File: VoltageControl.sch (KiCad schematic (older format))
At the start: 7 parts

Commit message: Initial Annotation
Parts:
- gave numbers to parts that had none: 7
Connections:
- net at R201.1, RV201.3: now also U201.3 (+); no longer U201.5 (+)
- net at R202.2, R203.1: now also U201.2 (-); no longer U201.6 (-)
- net at D201.2 (K): now also U201.1; no longer U201.7
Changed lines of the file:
@@
 $EndDescr
 $Comp
-L LMV358 U?
-U 2 1 54DB1D03
+L LMV358 U201
+U 1 1 54DB1D03
 P 5850 3050
-F 0 "U?" H 5800 3250 60  0000 L CNN
+F 0 "U201" H 5800 3250 60  0000 L CNN
 F 1 "LMV358" H 5800 2800 60  0000 L CNN
 F 2 "" H 5850 3050 60  0000 C CNN
 F 3 "" H 5850 3050 60  0000 C CNN
-	2    5850 3050
+	1    5850 3050
 	1    0    0    -1
 $EndComp
 $Comp
-L R R?
+L R R201
 U 1 1 54DB1D0A
 P 3950 4250
-F 0 "R?" V 4030 4250 50  0000 C CNN
+F 0 "R201" V 4030 4250 50  0000 C CNN
 F 1 "R" V 3957 4251 50  0000 C CNN
 F 2 "" V 3880 4250 30  0000 C CNN
@@
 $EndComp
 $Comp
-L GND #PWR?
+L GND #PWR202
 U 1 1 54DB1D11
 P 5750 3600
-F 0 "#PWR?" H 5750 3350 60  0001 C CNN
+F 0 "#PWR202" H 5750 3350 60  0001 C CNN
 F 1 "GND" H 5750 3450 60  0000 C CNN
 F 2 "" H 5750 3600 60  0000 C CNN
@@
 	3950 5550 9850 5550
 $Comp
-L POT RV?
+L POT RV201
 U 1 1 54DB1D22
 P 3950 3550
-F 0 "RV?" H 3950 3450 50  0000 C CNN
+F 0 "RV201" H 3950 3450 50  0000 C CNN
 F 1 "POT" H 3950 3550 50  0000 C CNN
 F 2 "" H 3950 3550 60  0000 C CNN
@@
 Connection ~ 4100 1950
 $Comp
-L GND #PWR?
+L GND #PWR201
 U 1 1 54DB1D2C
 P 5150 2650
-F 0 "#PWR?" H 5150 2400 60  0001 C CNN
+F 0 "#PWR201" H 5150 2400 60  0001 C CNN
 F 1 "GND" H 5150 2500 60  0000 C CNN
 F 2 "" H 5150 2650 60  0000 C CNN
@@
 $EndComp
 $Comp
-L C C?
+L C C201
 U 1 1 54DB1D32
 P 5150 2400
-F 0 "C?" H 5200 2500 50  0000 L CNN
+F 0 "C201" H 5200 2500 50  0000 L CNN
 F 1 "C" H 5200 2300 50  0000 L CNN
 F 2 "" H 5188 2250 30  0000 C CNN
@@
 	6350 3050 6550 3050
 $Comp
-L DIODE D?
+L DIODE D201
 U 1 1 54DB1E38
 P 6750 3050
-F 0 "D?" H 6750 3150 40  0000 C CNN
+F 0 "D201" H 6750 3150 40  0000 C CNN
 F 1 "DIODE" H 6750 2950 40  0000 C CNN
 F 2 "" H 6750 3050 60  0000 C CNN
@@
 $EndComp
 $Comp
-L R R?
+L R R202
 U 1 1 54DB1EC2
 P 8700 3450
-F 0 "R?" V 8780 3450 50  0000 C CNN
+F 0 "R202" V 8780 3450 50  0000 C CNN
 F 1 "9K" V 8707 3451 50  0000 C CNN
 F 2 "" V 8630 3450 30  0000 C CNN
@@
 $EndComp
 $Comp
-L R R?
+L R R203
 U 1 1 54DB1F3A
 P 8700 4300
-F 0 "R?" V 8780 4300 50  0000 C CNN
+F 0 "R203" V 8780 4300 50  0000 C CNN
 F 1 "1K" V 8707 4301 50  0000 C CNN
 F 2 "" V 8630 4300 30  0000 C CNN

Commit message: Preliminary association of components and placement into layout.
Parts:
- C201, R201, R202, R203: footprint (none) -> SMD_Packages:SMD-0805
- D201: footprint (none) -> SMD_Packages:SOD-523; MPN (none) -> 1N4148WT-7
- RV201: footprint (none) -> Potentiometers:Potentiometer_WirePads_largePads
- U201: footprint (none) -> SMD_Packages:SOIC-8-N; MPN (none) -> Value
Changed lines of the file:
@@
 F 0 "U201" H 5800 3250 60  0000 L CNN
 F 1 "LMV358" H 5800 2800 60  0000 L CNN
-F 2 "" H 5850 3050 60  0000 C CNN
-F 3 "" H 5850 3050 60  0000 C CNN
+F 2 "SMD_Packages:SOIC-8-N" H 5850 3050 60  0001 C CNN
+F 3 "" H 5850 3050 60  0001 C CNN
+F 4 "Value" H 5850 3050 60  0001 C CNN "MPN"
 	1    5850 3050
 	1    0    0    -1
@@
 F 0 "R201" V 4030 4250 50  0000 C CNN
 F 1 "R" V 3957 4251 50  0000 C CNN
-F 2 "" V 3880 4250 30  0000 C CNN
+F 2 "SMD_Packages:SMD-0805" V 3880 4250 30  0001 C CNN
 F 3 "" H 3950 4250 30  0000 C CNN
 	1    3950 4250
@@
 $EndComp
 $Comp
-L GND #PWR202
+L GND #PWR03
 U 1 1 54DB1D11
 P 5750 3600
-F 0 "#PWR202" H 5750 3350 60  0001 C CNN
+F 0 "#PWR03" H 5750 3350 60  0001 C CNN
 F 1 "GND" H 5750 3450 60  0000 C CNN
 F 2 "" H 5750 3600 60  0000 C CNN
@@
 F 0 "RV201" H 3950 3450 50  0000 C CNN
 F 1 "POT" H 3950 3550 50  0000 C CNN
-F 2 "" H 3950 3550 60  0000 C CNN
+F 2 "Potentiometers:Potentiometer_WirePads_largePads" H 3950 3550 60  0001 C CNN
 F 3 "" H 3950 3550 60  0000 C CNN
 	1    3950 3550
@@
 Connection ~ 4100 1950
 $Comp
-L GND #PWR201
+L GND #PWR04
 U 1 1 54DB1D2C
 P 5150 2650
-F 0 "#PWR201" H 5150 2400 60  0001 C CNN
+F 0 "#PWR04" H 5150 2400 60  0001 C CNN
 F 1 "GND" H 5150 2500 60  0000 C CNN
 F 2 "" H 5150 2650 60  0000 C CNN
@@
 F 0 "C201" H 5200 2500 50  0000 L CNN
 F 1 "C" H 5200 2300 50  0000 L CNN
-F 2 "" H 5188 2250 30  0000 C CNN
+F 2 "SMD_Packages:SMD-0805" H 5188 2250 30  0001 C CNN
 F 3 "" H 5150 2400 60  0000 C CNN
 	1    5150 2400
@@
 F 0 "D201" H 6750 3150 40  0000 C CNN
 F 1 "DIODE" H 6750 2950 40  0000 C CNN
-F 2 "" H 6750 3050 60  0000 C CNN
-F 3 "" H 6750 3050 60  0000 C CNN
+F 2 "SMD_Packages:SOD-523" H 6750 3050 60  0001 C CNN
+F 3 "http://www.diodes.com/datasheets/ds30396.pdf" H 6750 3050 60  0001 C CNN
+F 4 "1N4148WT-7" H 6750 3050 60  0001 C CNN "MPN"
 	1    6750 3050
 	-1   0    0    1
@@
 F 0 "R202" V 8780 3450 50  0000 C CNN
 F 1 "9K" V 8707 3451 50  0000 C CNN
-F 2 "" V 8630 3450 30  0000 C CNN
+F 2 "SMD_Packages:SMD-0805" V 8630 3450 30  0001 C CNN
 F 3 "" H 8700 3450 30  0000 C CNN
 	1    8700 3450
@@
 F 0 "R203" V 8780 4300 50  0000 C CNN
 F 1 "1K" V 8707 4301 50  0000 C CNN
-F 2 "" V 8630 4300 30  0000 C CNN
+F 2 "SMD_Packages:SMD-0805" V 8630 4300 30  0001 C CNN
 F 3 "" H 8700 4300 30  0000 C CNN
 	1    8700 4300

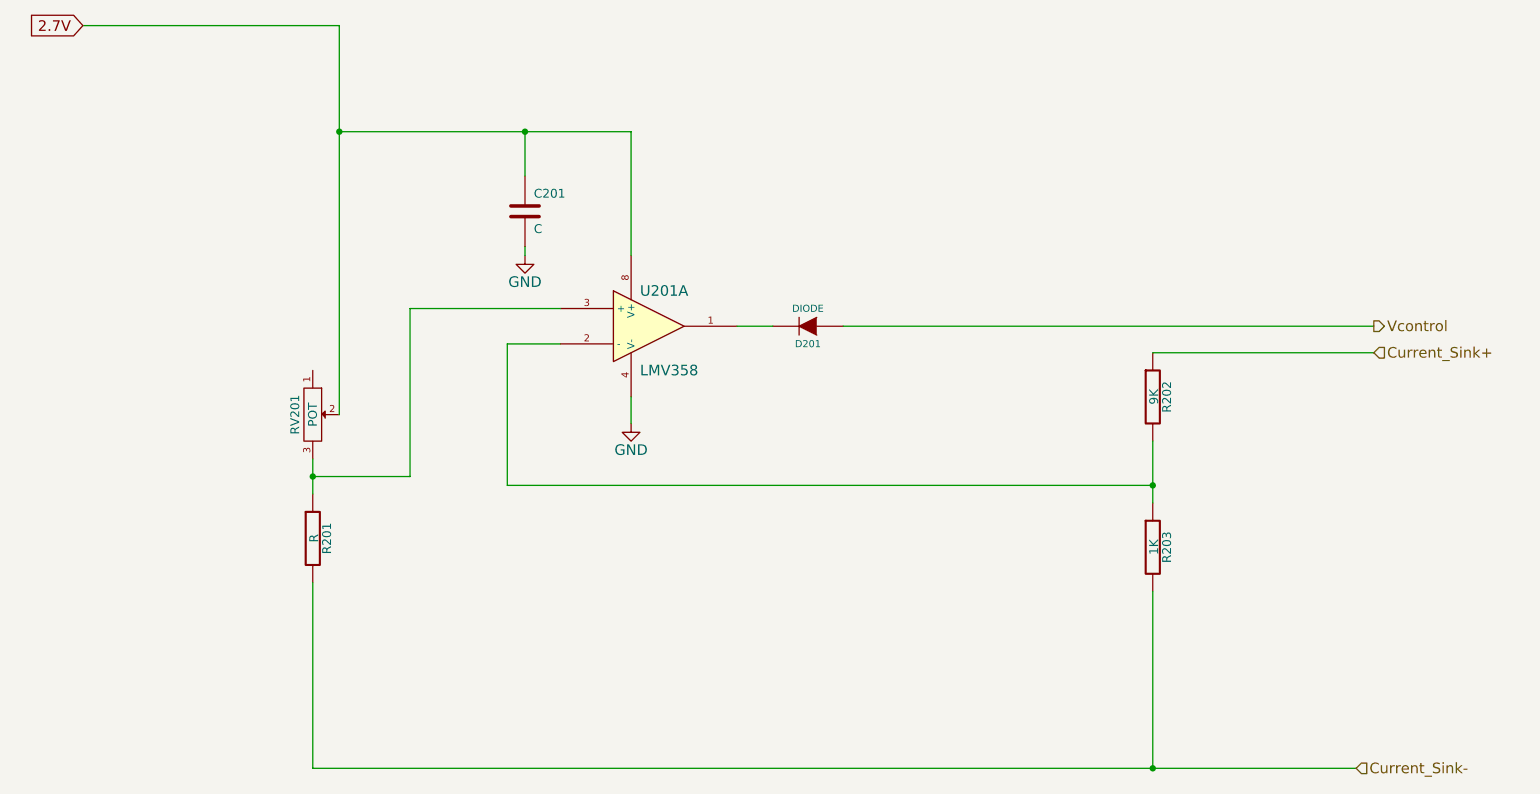
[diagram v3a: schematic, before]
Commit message: Fixed divider resistors and found values
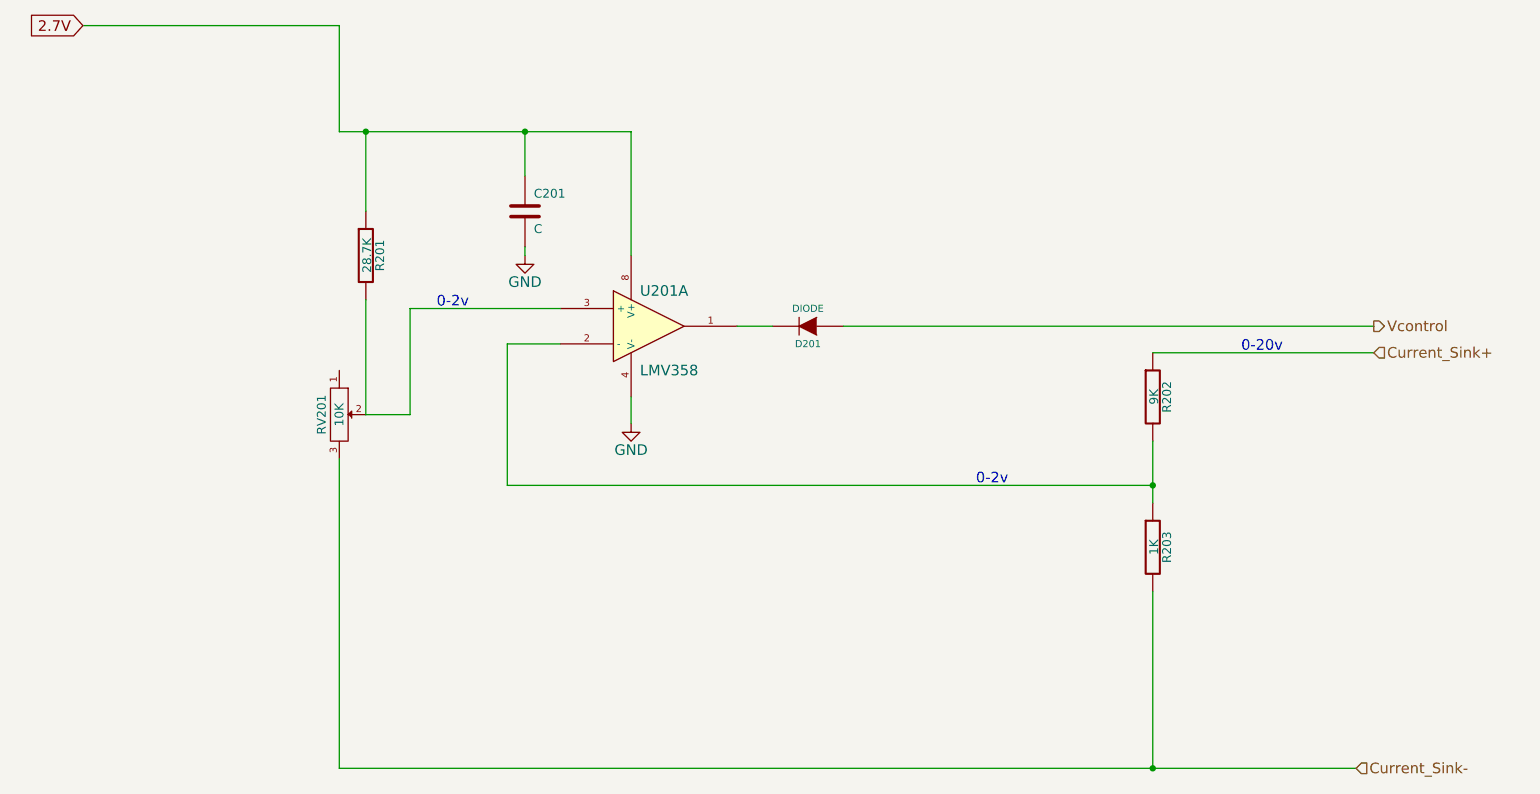
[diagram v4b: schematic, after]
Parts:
- R201: value R -> 28.7K
- RV201: value POT -> 10K; footprint Potentiometers:Potentiometer_WirePads_largePads -> Current:P090L-02F25BR10K; MPN (none) -> P090L-02F25BR10K
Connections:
- net 2.7V: now also R201.1; no longer RV201.2
- net Current_Sink-: now also RV201.3; no longer R201.2
- new net: R201.2, RV201.2, U201.3 (+)
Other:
- note added: "0-20v"
- note added: "0-2v"
- moved on the sheet: R201, RV201
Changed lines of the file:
@@
 L R R201
 U 1 1 54DB1D0A
-P 3950 4250
-F 0 "R201" V 4030 4250 50  0000 C CNN
-F 1 "R" V 3957 4251 50  0000 C CNN
-F 2 "SMD_Packages:SMD-0805" V 3880 4250 30  0001 C CNN
-F 3 "" H 3950 4250 30  0000 C CNN
-	1    3950 4250
+P 4250 2650
+F 0 "R201" V 4330 2650 50  0000 C CNN
+F 1 "28.7K" V 4257 2651 50  0000 C CNN
+F 2 "SMD_Packages:SMD-0805" V 4180 2650 30  0001 C CNN
+F 3 "" H 4250 2650 30  0000 C CNN
+	1    4250 2650
 	1    0    0    -1
 $EndComp
@@
 	5350 2950 4500 2950
 Wire Wire Line
-	4500 2950 4500 3900
+	4100 3800 4100 5550
 Wire Wire Line
-	4500 3900 3950 3900
-Connection ~ 3950 3900
-Wire Wire Line
-	3950 4500 3950 5550
-Wire Wire Line
-	3950 5550 9850 5550
+	4100 5550 9850 5550
 $Comp
 L POT RV201
 U 1 1 54DB1D22
-P 3950 3550
-F 0 "RV201" H 3950 3450 50  0000 C CNN
-F 1 "POT" H 3950 3550 50  0000 C CNN
-F 2 "Potentiometers:Potentiometer_WirePads_largePads" H 3950 3550 60  0001 C CNN
-F 3 "" H 3950 3550 60  0000 C CNN
-	1    3950 3550
+P 4100 3550
+F 0 "RV201" H 4100 3450 50  0000 C CNN
+F 1 "10K" H 4100 3550 50  0000 C CNN
+F 2 "Current:P090L-02F25BR10K" H 4100 3550 60  0001 C CNN
+F 3 "" H 4100 3550 60  0000 C CNN
+F 4 "P090L-02F25BR10K" H 4100 3550 60  0001 C CNN "MPN"
+	1    4100 3550
 	0    1    1    0
 $EndComp
 Wire Wire Line
-	4100 1950 5750 1950
-Wire Wire Line
 	5750 1950 5750 2650
-Connection ~ 4100 1950
 $Comp
 L GND #PWR04
@@
 $EndComp
 Wire Wire Line
-	5150 2200 5150 1950
+	5150 1950 5150 2200
 Connection ~ 5150 1950
 Wire Wire Line
@@
 Wire Wire Line
 	2650 1350 4100 1350
-Wire Wire Line
-	4100 1350 4100 3550
 Wire Wire Line
 	6350 3050 6550 3050
@@
 Connection ~ 8700 5550
 Wire Wire Line
-	3950 3800 3950 4000
+	4500 3550 4250 3550
+Wire Wire Line
+	4250 3550 4250 2900
+Wire Wire Line
+	4100 1350 4100 1950
+Wire Wire Line
+	4250 1950 4250 2400
+Connection ~ 4250 1950
+Wire Wire Line
+	4100 1950 5750 1950
+Wire Wire Line
+	4500 2950 4500 3550
+Text Notes 4650 2950 0    60   ~ 0
+0-2v
+Text Notes 7700 3950 0    60   ~ 0
+0-2v
+Text Notes 9200 3200 0    60   ~ 0
+0-20v
 $EndSCHEMATC

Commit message: Cosmetic cleanup of schematic
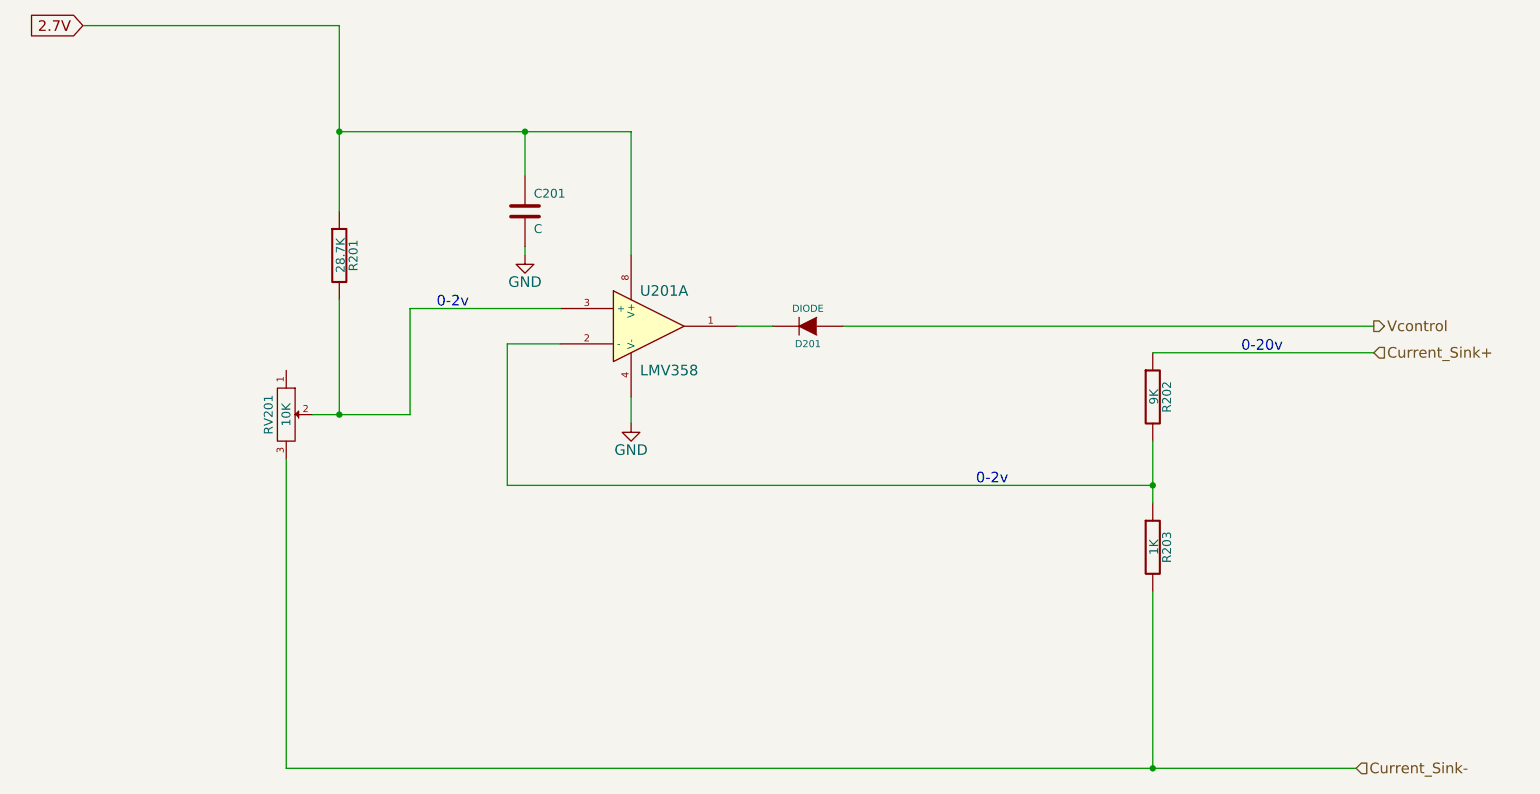
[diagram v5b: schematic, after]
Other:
- moved on the sheet: R201, RV201
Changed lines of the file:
@@
 L R R201
 U 1 1 54DB1D0A
-P 4250 2650
-F 0 "R201" V 4330 2650 50  0000 C CNN
-F 1 "28.7K" V 4257 2651 50  0000 C CNN
-F 2 "SMD_Packages:SMD-0805" V 4180 2650 30  0001 C CNN
-F 3 "" H 4250 2650 30  0000 C CNN
-	1    4250 2650
+P 4100 2650
+F 0 "R201" V 4180 2650 50  0000 C CNN
+F 1 "28.7K" V 4107 2651 50  0000 C CNN
+F 2 "SMD_Packages:SMD-0805" V 4030 2650 30  0001 C CNN
+F 3 "" H 4100 2650 30  0000 C CNN
+	1    4100 2650
 	1    0    0    -1
 $EndComp
@@
 	5350 2950 4500 2950
 Wire Wire Line
-	4100 3800 4100 5550
+	3800 3800 3800 5550
 Wire Wire Line
-	4100 5550 9850 5550
+	3800 5550 9850 5550
 $Comp
 L POT RV201
 U 1 1 54DB1D22
-P 4100 3550
-F 0 "RV201" H 4100 3450 50  0000 C CNN
-F 1 "10K" H 4100 3550 50  0000 C CNN
-F 2 "Current:P090L-02F25BR10K" H 4100 3550 60  0001 C CNN
-F 3 "" H 4100 3550 60  0000 C CNN
-F 4 "P090L-02F25BR10K" H 4100 3550 60  0001 C CNN "MPN"
-	1    4100 3550
+P 3800 3550
+F 0 "RV201" H 3800 3450 50  0000 C CNN
+F 1 "10K" H 3800 3550 50  0000 C CNN
+F 2 "Current:P090L-02F25BR10K" H 3800 3550 60  0001 C CNN
+F 3 "" H 3800 3550 60  0000 C CNN
+F 4 "P090L-02F25BR10K" H 3800 3550 60  0001 C CNN "MPN"
+	1    3800 3550
 	0    1    1    0
 $EndComp
@@
 Connection ~ 8700 5550
 Wire Wire Line
-	4500 3550 4250 3550
+	4500 3550 3950 3550
 Wire Wire Line
-	4250 3550 4250 2900
-Wire Wire Line
-	4100 1350 4100 1950
-Wire Wire Line
-	4250 1950 4250 2400
-Connection ~ 4250 1950
+	4100 1350 4100 2400
+Connection ~ 4100 1950
 Wire Wire Line
 	4100 1950 5750 1950
@@
 Text Notes 9200 3200 0    60   ~ 0
 0-20v
+Wire Wire Line
+	4100 2900 4100 3550
+Connection ~ 4100 3550
 $EndSCHEMATC

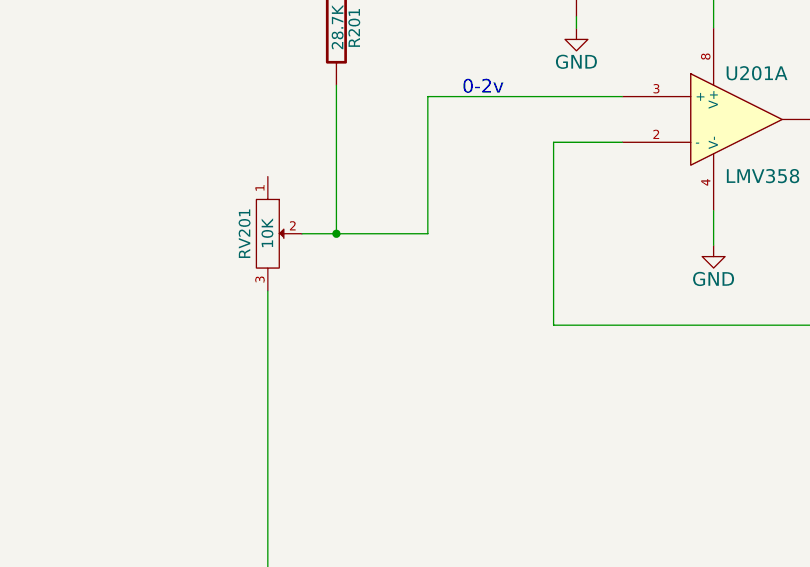
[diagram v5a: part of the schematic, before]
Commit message: added measure pins and ripup layout
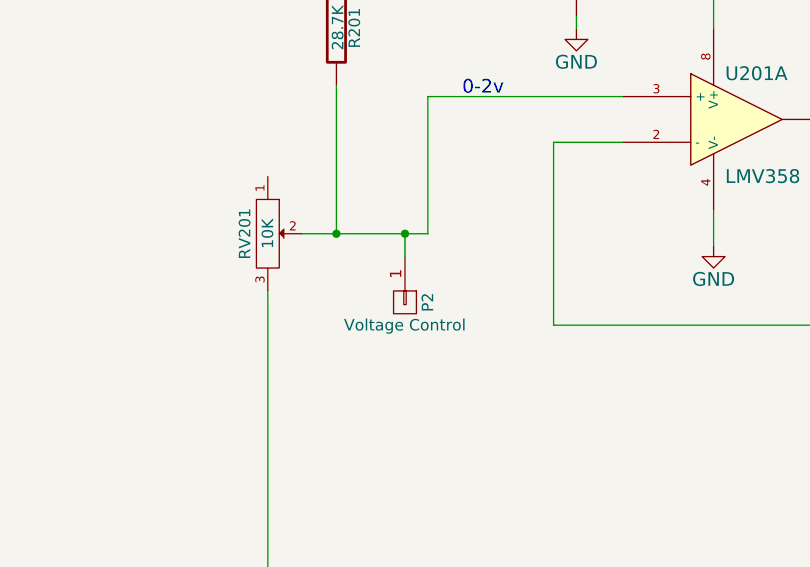
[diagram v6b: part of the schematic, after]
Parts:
- added P2: Voltage Control, symbol CONN_01X01
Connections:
- net at R201.2, RV201.2, U201.3 (+): now also P2.1 (P1)
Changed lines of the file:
@@
 $EndComp
 $Comp
-L GND #PWR03
+L GND #PWR5
 U 1 1 54DB1D11
 P 5750 3600
-F 0 "#PWR03" H 5750 3350 60  0001 C CNN
+F 0 "#PWR5" H 5750 3350 60  0001 C CNN
 F 1 "GND" H 5750 3450 60  0000 C CNN
 F 2 "" H 5750 3600 60  0000 C CNN
@@
 	5750 1950 5750 2650
 $Comp
-L GND #PWR04
+L GND #PWR4
 U 1 1 54DB1D2C
 P 5150 2650
-F 0 "#PWR04" H 5150 2400 60  0001 C CNN
+F 0 "#PWR4" H 5150 2400 60  0001 C CNN
 F 1 "GND" H 5150 2500 60  0000 C CNN
 F 2 "" H 5150 2650 60  0000 C CNN
@@
 	4100 2900 4100 3550
 Connection ~ 4100 3550
+$Comp
+L CONN_01X01 P2
+U 1 1 54F1F52A
+P 4400 3850
+F 0 "P2" H 4400 3950 50  0000 C CNN
+F 1 "Voltage Control" V 4500 3850 50  0000 C CNN
+F 2 "" H 4400 3850 60  0000 C CNN
+F 3 "" H 4400 3850 60  0000 C CNN
+	1    4400 3850
+	0    1    1    0
+$EndComp
+Wire Wire Line
+	4400 3650 4400 3550
+Connection ~ 4400 3550
 $EndSCHEMATC

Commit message: Changed footprints, changed layout
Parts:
- P2: value Voltage Control -> V; footprint (none) -> Pin_Headers:Pin_Header_Straight_1x01
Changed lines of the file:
@@
 $EndComp
 $Comp
-L GND #PWR5
+L GND #PWR04
 U 1 1 54DB1D11
 P 5750 3600
-F 0 "#PWR5" H 5750 3350 60  0001 C CNN
+F 0 "#PWR04" H 5750 3350 60  0001 C CNN
 F 1 "GND" H 5750 3450 60  0000 C CNN
 F 2 "" H 5750 3600 60  0000 C CNN
@@
 	5750 1950 5750 2650
 $Comp
-L GND #PWR4
+L GND #PWR05
 U 1 1 54DB1D2C
 P 5150 2650
-F 0 "#PWR4" H 5150 2400 60  0001 C CNN
+F 0 "#PWR05" H 5150 2400 60  0001 C CNN
 F 1 "GND" H 5150 2500 60  0000 C CNN
 F 2 "" H 5150 2650 60  0000 C CNN
@@
 P 4400 3850
 F 0 "P2" H 4400 3950 50  0000 C CNN
-F 1 "Voltage Control" V 4500 3850 50  0000 C CNN
-F 2 "" H 4400 3850 60  0000 C CNN
+F 1 "V" V 4500 3850 50  0000 C CNN
+F 2 "Pin_Headers:Pin_Header_Straight_1x01" H 4400 3850 60  0001 C CNN
 F 3 "" H 4400 3850 60  0000 C CNN
 	1    4400 3850
